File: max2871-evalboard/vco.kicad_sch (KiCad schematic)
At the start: 44 parts

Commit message: Finish schematic - create PCB
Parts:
- removed C? (x3): 2.2uF, Capacitor_SMD:C_0603_1608Metric, symbol Device:C
- removed C?: 1uF, Capacitor_SMD:C_0402_1005Metric, symbol Device:C
- removed C?: 100pF, Capacitor_SMD:C_0402_1005Metric, symbol Device:C
- removed C?: 10nF, Capacitor_SMD:C_0402_1005Metric, symbol Device:C
- removed C?: 100nF, Capacitor_SMD:C_0402_1005Metric, symbol Device:C
- removed J?: Conn_01x02, Connector_PinHeader_2.54mm:PinHeader_2x01_P2.54mm_Horizontal, symbol Connector_Generic:Conn_01x02
- removed L?: BLM18PG181S, Inductor_SMD:L_0603_1608Metric, symbol Device:L_Ferrite_Small
- removed R?: 1k, Resistor_SMD:R_0402_1005Metric, symbol Device:R
- removed R?: 10k, Resistor_SMD:R_0402_1005Metric, symbol Device:R
- removed U?: MAX8559ETAAAT, MAX8559ETAAAT:SON65P300X300X80-9N, symbol MAX8559ETAAAT:MAX8559ETAAAT
- added C301, C302, C303, C309, C310, C311, C312: 1uF, Capacitor_SMD:C_0402_1005Metric, symbol Device:C
- added R301, R303, R310: 1k, Resistor_SMD:R_0402_1005Metric, symbol Device:R
- added R307: 0, Resistor_SMD:R_0402_1005Metric, symbol Device:R
- added R308, R309: DNP, Resistor_SMD:R_0402_1005Metric, symbol Device:R
- added TP301, TP302, TP303, TP304, TP305: (no value), TestPoint:TestPoint_Pad_D1.5mm, symbol Connector:TestPoint
- added U301, U302: LP5907MFX-3.3, Package_TO_SOT_SMD:SOT-23-5, symbol Regulator_Linear:LP5907MFX-3.3
- added U303: LP5907MFX-1.8, Package_TO_SOT_SMD:SOT-23-5, symbol Regulator_Linear:LP5907MFX-1.8
- C304, C306, C313, C314, C315: renamed from C?; Partnumber (none) -> CL05F104ZO5NNNC
- C305, C319, C320, C323: renamed from C?; LCSC (none) -> C126521; Manufacturer (none) -> Murata; Part Number (none) -> GCM155C71A105KE38D; Partnumber (none) -> GCM155C71A105KE38D
- C307: renamed from C?; LCSC (none) -> C113786; Manufacturer (none) -> YAGEO; Part Number (none) -> CC0402KRX7R8BB123; Partnumber (none) -> CC0402KRX7R8BB123
- C308: renamed from C?; LCSC (none) -> C107031; Manufacturer (none) -> YAGEO; Part Number (none) -> CC0402KRX7R9BB821; Partnumber (none) -> CC0402KRX7R9BB821
- C316, C317, C318, C324, C325: renamed from C?; Partnumber (none) -> CC0402KRX7R7BB101
- C321, C322: renamed from C?; Partnumber (none) -> TMK105B7103KVHF
- L301: renamed from L?; Partnumber (none) -> BLM18PG181SH1D
- R302: renamed from R?; LCSC (none) -> C705665; Manufacturer (none) -> YAGEO; Part Number (none) -> RT0402CRE071KL; Partnumber (none) -> RT0402CRE071KL
- R304: renamed from R?; LCSC (none) -> C852950; Manufacturer (none) -> YAGEO; Part Number (none) -> RT0402BRD0790R9L; Partnumber (none) -> RT0402BRD0790R9L
- R305, R306, R316, R317: renamed from R?; Partnumber (none) -> PTFR0402B49R9N9
- R311, R312, R315: renamed from R?; LCSC (none) -> C351692; Manufacturer (none) -> Resistor Today; Part Number (none) -> PTFR0402B5K10N9; Partnumber (none) -> PTFR0402B5K10N9
- R313, R314: renamed from R?; Partnumber (none) -> PA0402-R-070RL
- U304: renamed from U?; Partnumber (none) -> O3254000153350
- gave numbers to parts that had none: 1
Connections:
- net GND: now also C301.2, C302.2, C303.2, C309.2, C310.2, C311.2, C312.2, U301.2 (GND), U302.2 (GND), U303.2 (GND)
- net VCC_DIG: now also C309.1, R308.1, TP301.1
- net VCC_PLL: now also C312.1, TP303.1, U302.5 (OUT)
- net VCC_TXCO: now also R307.2, R308.2, R310.2, TP304.1, TP305.1
- net VCC_VCO: now also C311.1, TP302.1, U301.5 (OUT)
- net VIN: now also C301.1, C302.1, C303.1, R301.1, R303.1, U301.1 (IN), U302.1 (IN), U303.1 (IN)
- net EN_TXCO: now reaches U304.1 (E/D)
- net EN_TXCO: now also R309.1
- net at R302.2: now also U302.3 (EN)
- new net: C310.1, R307.1, U303.5 (OUT)
- new net: R303.2, U303.3 (EN)
- new net: R301.2, U301.3 (EN)
- new net TXCO_PWR: R309.2, R310.1
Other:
- note added: "Clock source"
- note added: "Place decoupling caps C314 and C317 close to pins 16 and 17."
- note added: "Place decoupling caps C315 and C318 close to pins 6 and 10."
- note removed: "Place decoupling caps Ca and Cb close to pins 16 and 17."
- note removed: "Place decoupling caps Cc and Cd close to pins 6 and 10."
- moved on the sheet: C304, C305, C306, C307, C308, C313, C314, C315, C316, C317, C318, C319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

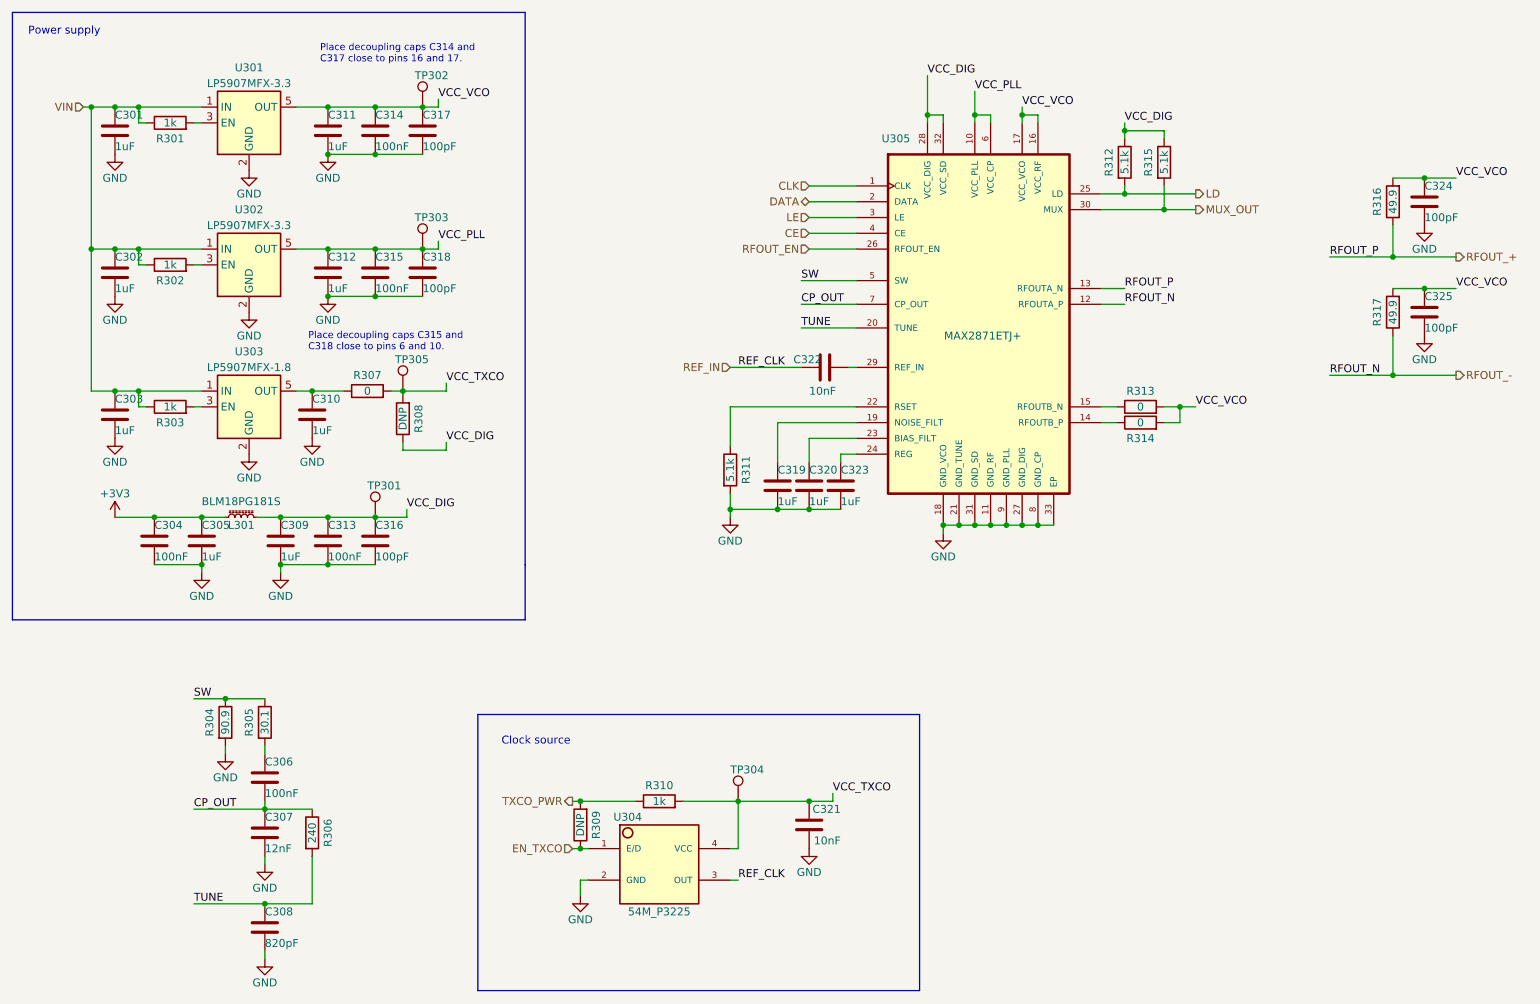
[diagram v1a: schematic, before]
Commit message: PCB placement complete
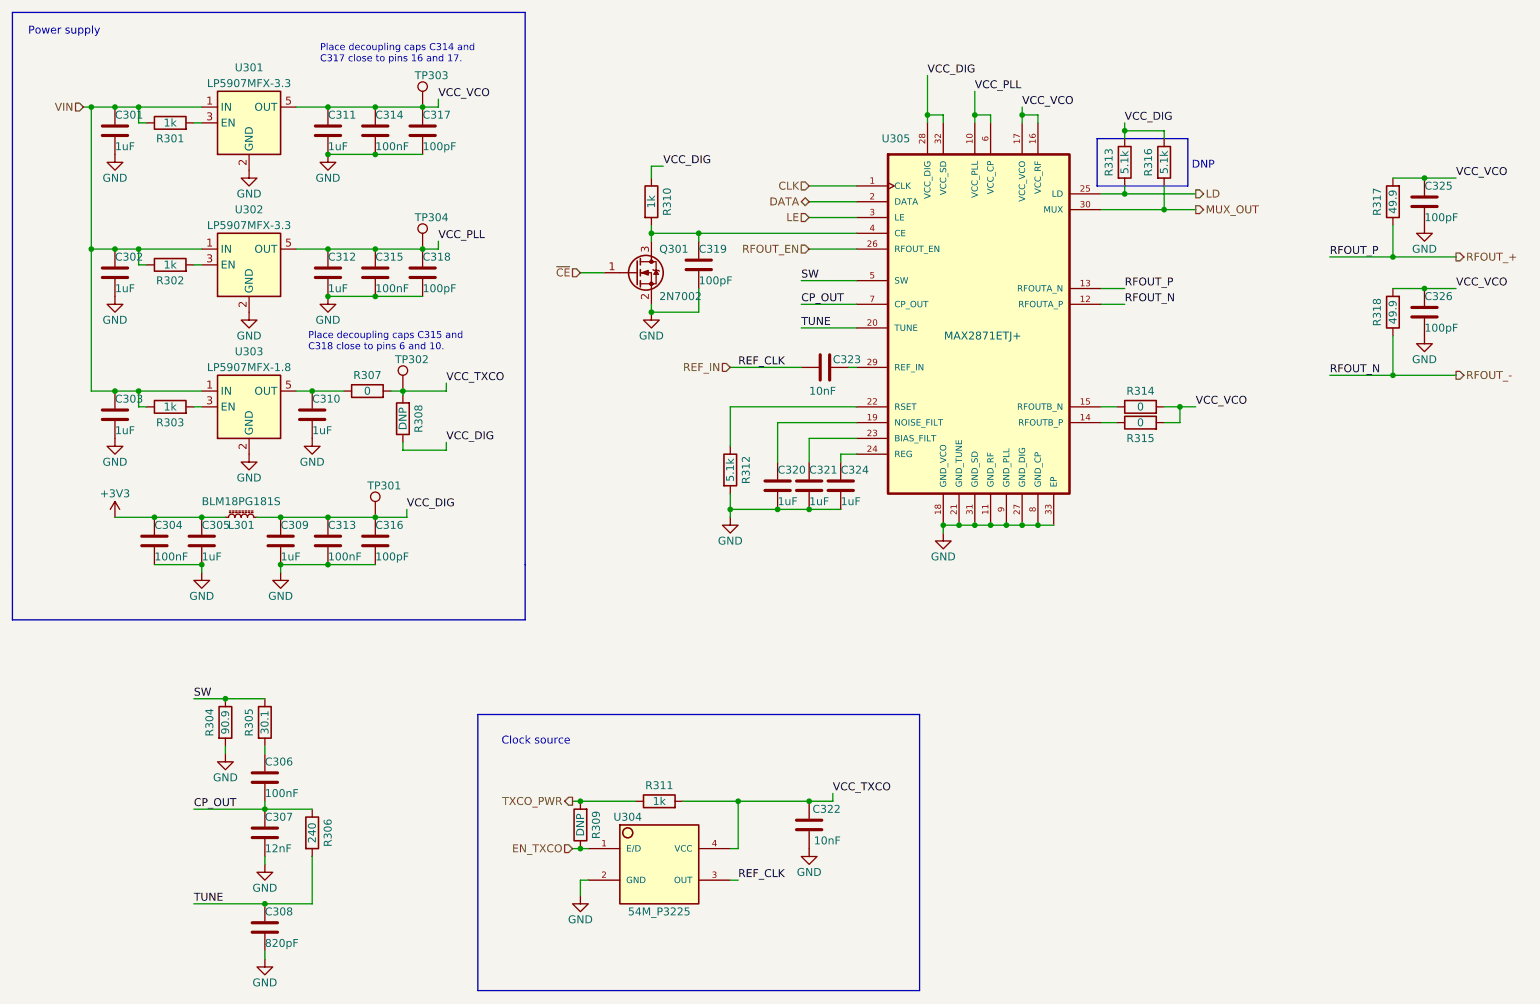
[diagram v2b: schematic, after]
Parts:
- removed TP304: (no value), TestPoint:TestPoint_Pad_D1.5mm, symbol Connector:TestPoint
- added C319: 100pF, Capacitor_SMD:C_0402_1005Metric, symbol Device:C
- added Q301: 2N7002, Package_TO_SOT_SMD:SOT-23, symbol Transistor_FET:2N7002
- added R310: 1k, Resistor_SMD:R_0402_1005Metric, symbol Device:R
- R309: footprint Resistor_SMD:R_0402_1005Metric -> Resistor_SMD:R_0603_1608Metric
- renumbered C319 to C320, C320 to C321, C321 to C322, C322 to C323, C323 to C324, C324 to C325, C325 to C326, R310 to R311, R311 to R312, R312 to R313, R313 to R314, R314 to R315, R315 to R316, R316 to R317, R317 to R318, TP305 to TP302, TP302 to TP303, TP303 to TP304
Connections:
- net GND: now also C319.2, Q301.2 (S)
- net VCC_DIG: now also R310.1
- net CE: no longer names the net of U305.4 (CE)
- net CE: now also C319.1, Q301.3 (D), R310.2
- new net ~{CE}: Q301.1 (G)
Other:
- note added: "DNP"

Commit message: Finish layout design
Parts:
- removed C302, C303, C310, C312: 1uF, Capacitor_SMD:C_0402_1005Metric, symbol Device:C
- removed R302, R303: 1k, Resistor_SMD:R_0402_1005Metric, symbol Device:R
- removed R308: DNP, Resistor_SMD:R_0402_1005Metric, symbol Device:R
- removed TP302: (no value), TestPoint:TestPoint_Pad_D1.5mm, symbol Connector:TestPoint
- removed U302: LP5907MFX-3.3, Package_TO_SOT_SMD:SOT-23-5, symbol Regulator_Linear:LP5907MFX-3.3
- removed U303: LP5907MFX-1.8, Package_TO_SOT_SMD:SOT-23-5, symbol Regulator_Linear:LP5907MFX-1.8
- added C304, C305: 100nF, Capacitor_SMD:C_0402_1005Metric, symbol Device:C
- added C315, C316: 100pF, Capacitor_SMD:C_0402_1005Metric, symbol Device:C
- added L301, L302: BLM18PG181S, Inductor_SMD:L_0603_1608Metric, symbol Device:L_Ferrite_Small
- renumbered C304 to C302, C305 to C303, C314 to C306, C315 to C307, C306 to C308, C307 to C309, C308 to C310, C309 to C311, C317 to C312, C318 to C313, C313 to C314, C311 to C317, C316 to C318, L301 to L303, R304 to R302, R307 to R303, R305 to R304, R306 to R305, R309 to R306, R310 to R307, R311 to R308, R312 to R309, R313 to R310, R314 to R311, R315 to R312, R316 to R313, R317 to R314, R318 to R315, TP303 to TP301, TP304 to TP302, TP301 to TP303, U304 to U302, U305 to U303
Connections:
- net GND: now also C304.2, C305.2, C315.2, C316.2
- net VCC_DIG: now also R303.1
- net VCC_PLL: now also C305.1, C316.1, L302.2
- net VCC_VCO: now also C304.1, C315.1, L301.2; no longer C317.1, U301.5 (OUT)
- new net: C317.1, L301.1, L302.1, U301.5 (OUT)
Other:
- moved on the sheet: C301, C302, C303, C306, C307, C311, C312, C313, C314, C317, C318, L303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
